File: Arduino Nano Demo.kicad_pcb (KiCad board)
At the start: 2 copper layers, 60 x 62 mm, 26 parts, among them J1 Barrel_Jack, J2 Conn_01x01_Female, J3 Conn_01x01_Female, P1 Digital, P2 Analog, P3 CONN_01X01, P4 CONN_01X01, P5 CONN_01X01, P6 CONN_01X01, SW1 SW_SPST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

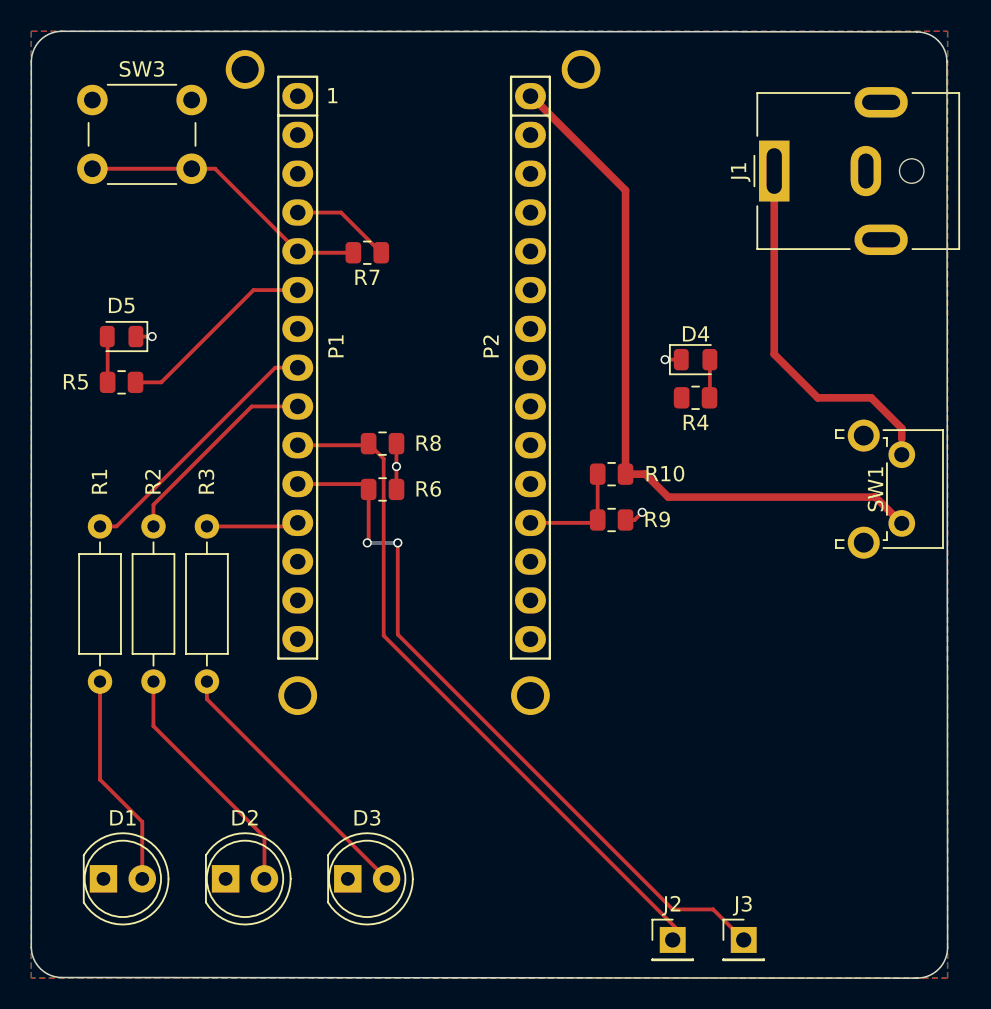
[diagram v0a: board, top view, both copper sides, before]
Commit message: Added JST connectors
Found some nice JST plugs to add for the inputs; makes more sense to have grounds for them anyway. Cool 3D models and everything.
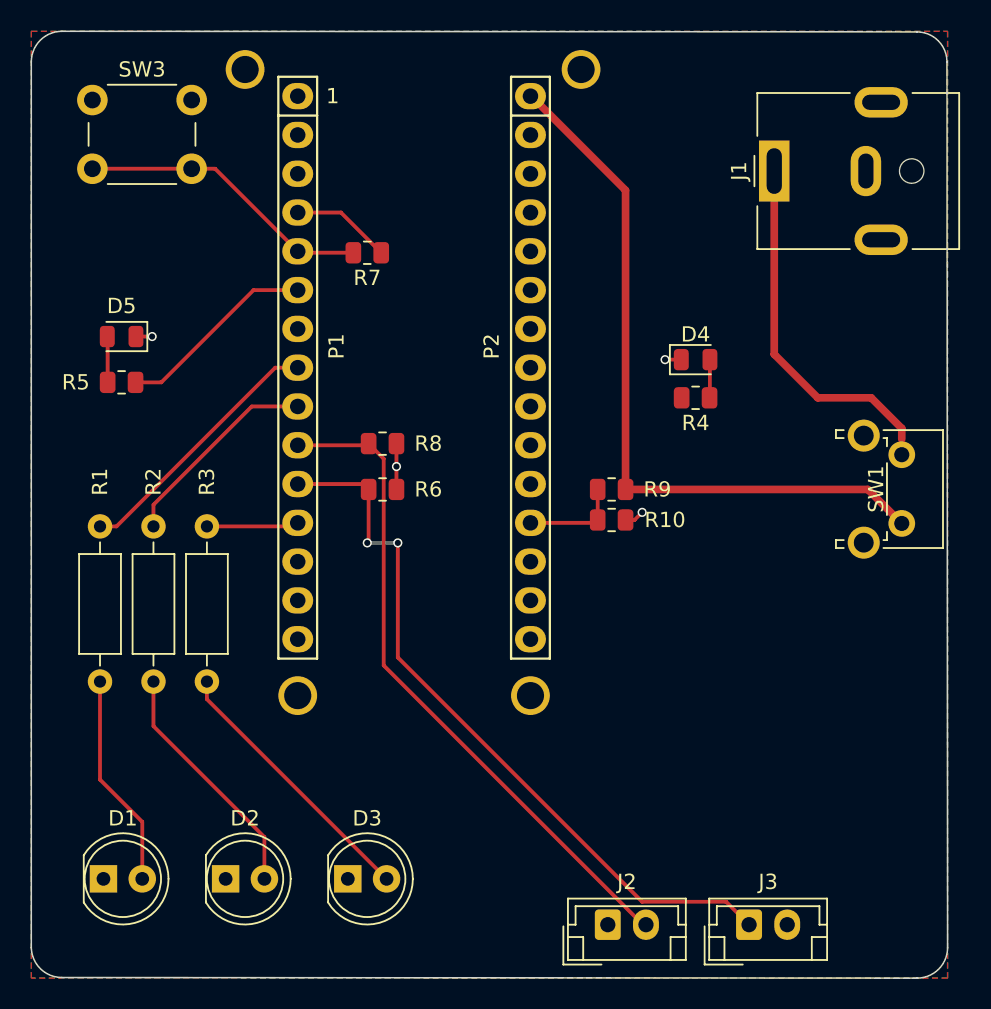
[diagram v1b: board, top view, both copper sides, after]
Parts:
- J2, J3: value Conn_01x01_Female -> Conn_01x02_Female; footprint Connector_PinHeader_2.54mm:PinHeader_1x01_P2.54mm_Vertical -> Connector_JST:JST_EH_B2B-EH-A_1x02_P2.50mm_Vertical
- moved J2 4.37 mm to (159.8, 125.5)
- moved J3 1.06 mm to (169.0, 125.5)
- moved R9 1.00 mm to (160.0, 97.0)
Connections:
- J2 pad 1: /7 -> GND
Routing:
- net /A0: track 7.48 -> 6.48 mm
- net /8: track 47.3 -> 48.1 mm
- net /7: track 44.9 -> 44.1 mm
- net /Vin: track 46.8 -> 47.4 mm
